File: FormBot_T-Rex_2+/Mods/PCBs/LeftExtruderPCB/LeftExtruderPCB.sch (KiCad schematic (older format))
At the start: 8 parts, among them J1 DB15_Control, J2 BL-2, J3 BL-3, J4 FAN_CTL, J5 FAN_AO, J6 EO, J7 Stepper, J8 HEAT

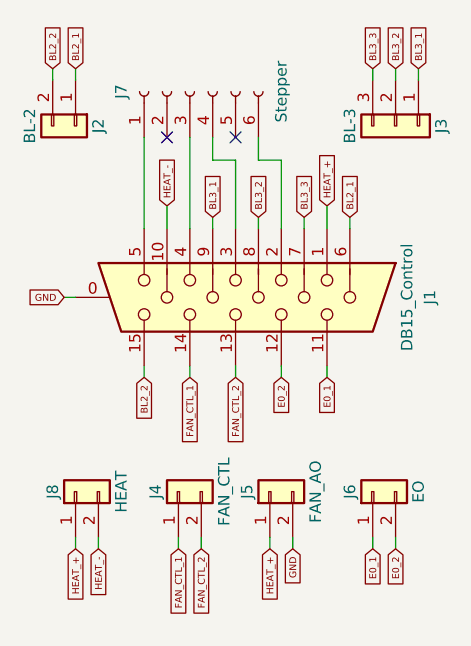
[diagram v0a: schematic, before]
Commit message: Adding right extruder PCB
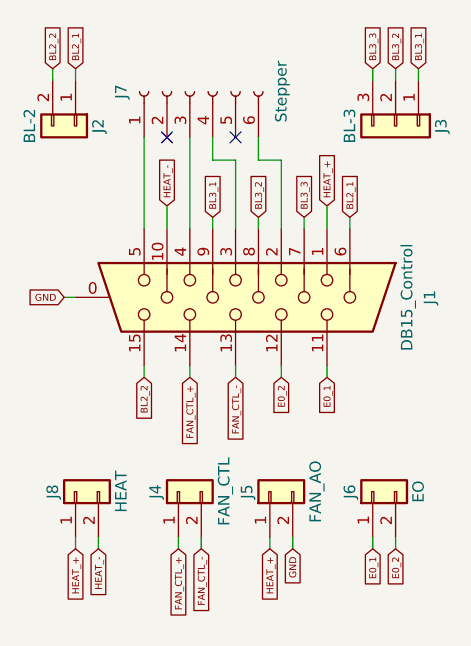
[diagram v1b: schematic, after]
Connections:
- net FAN_CTL_1 renamed FAN_CTL_+
- net FAN_CTL_2 renamed FAN_CTL_-
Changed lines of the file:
@@
 LIBS:contrib
 LIBS:valves
+LIBS:LeftExtruderPCB-cache
 EELAYER 25 0
 EELAYER END
@@
 HEAT_-
 Text GLabel 4150 2450 3    30   Input ~ 0
-FAN_CTL_2
+FAN_CTL_-
 Text GLabel 4000 3200 3    30   Input ~ 0
-FAN_CTL_2
+FAN_CTL_-
 Text GLabel 3950 2450 3    30   Input ~ 0
-FAN_CTL_1
+FAN_CTL_+
 Text GLabel 3900 3200 3    30   Input ~ 0
-FAN_CTL_1
+FAN_CTL_+
 Text GLabel 4550 2450 3    30   Input ~ 0
 E0_1
